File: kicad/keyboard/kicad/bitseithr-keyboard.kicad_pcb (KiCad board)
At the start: 4 copper layers, 365 x 206 mm, 105 parts, among them P2 KEYB CONN 1

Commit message: removed inner layers, added ground plane on bottom
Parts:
- removed U? (x2): SW-TH_EC11E1820402, clholm-kicad-library:SW-TH_EC11E1820402
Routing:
- net GND: track 244.3 -> 217.0 mm, vias 0 -> 2
- net +9V: track 387.4 -> 375.4 mm, vias 3 -> 1
- net COL6: track 226.5 -> 216.3 mm
- net ROW5: track 115.9 -> 106.4 mm
- net ROW3: track 507.2 -> 498.7 mm
- added copper zone on B.Cu, net GND
- removed copper zone on In1.Cu, net (none)
- removed copper zone on In2.Cu, net (none)
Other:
- copper layers 4 -> 2

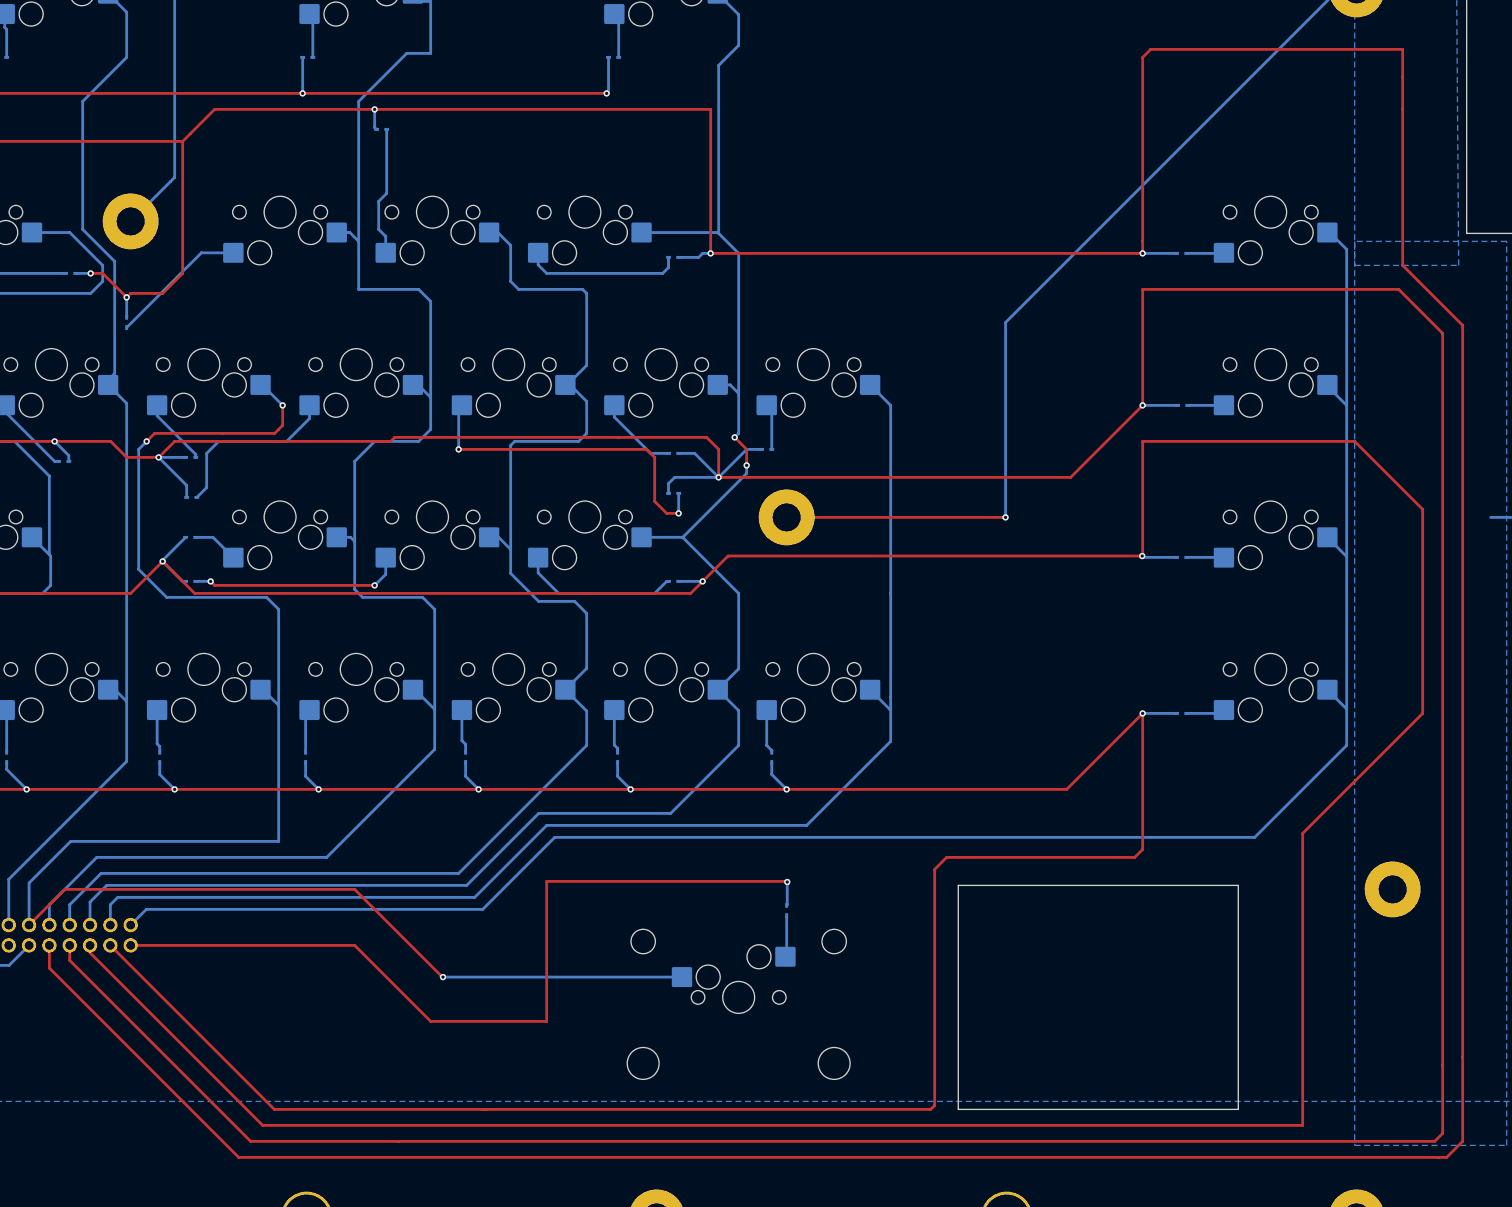
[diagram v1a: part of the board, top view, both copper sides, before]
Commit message: some routing updates
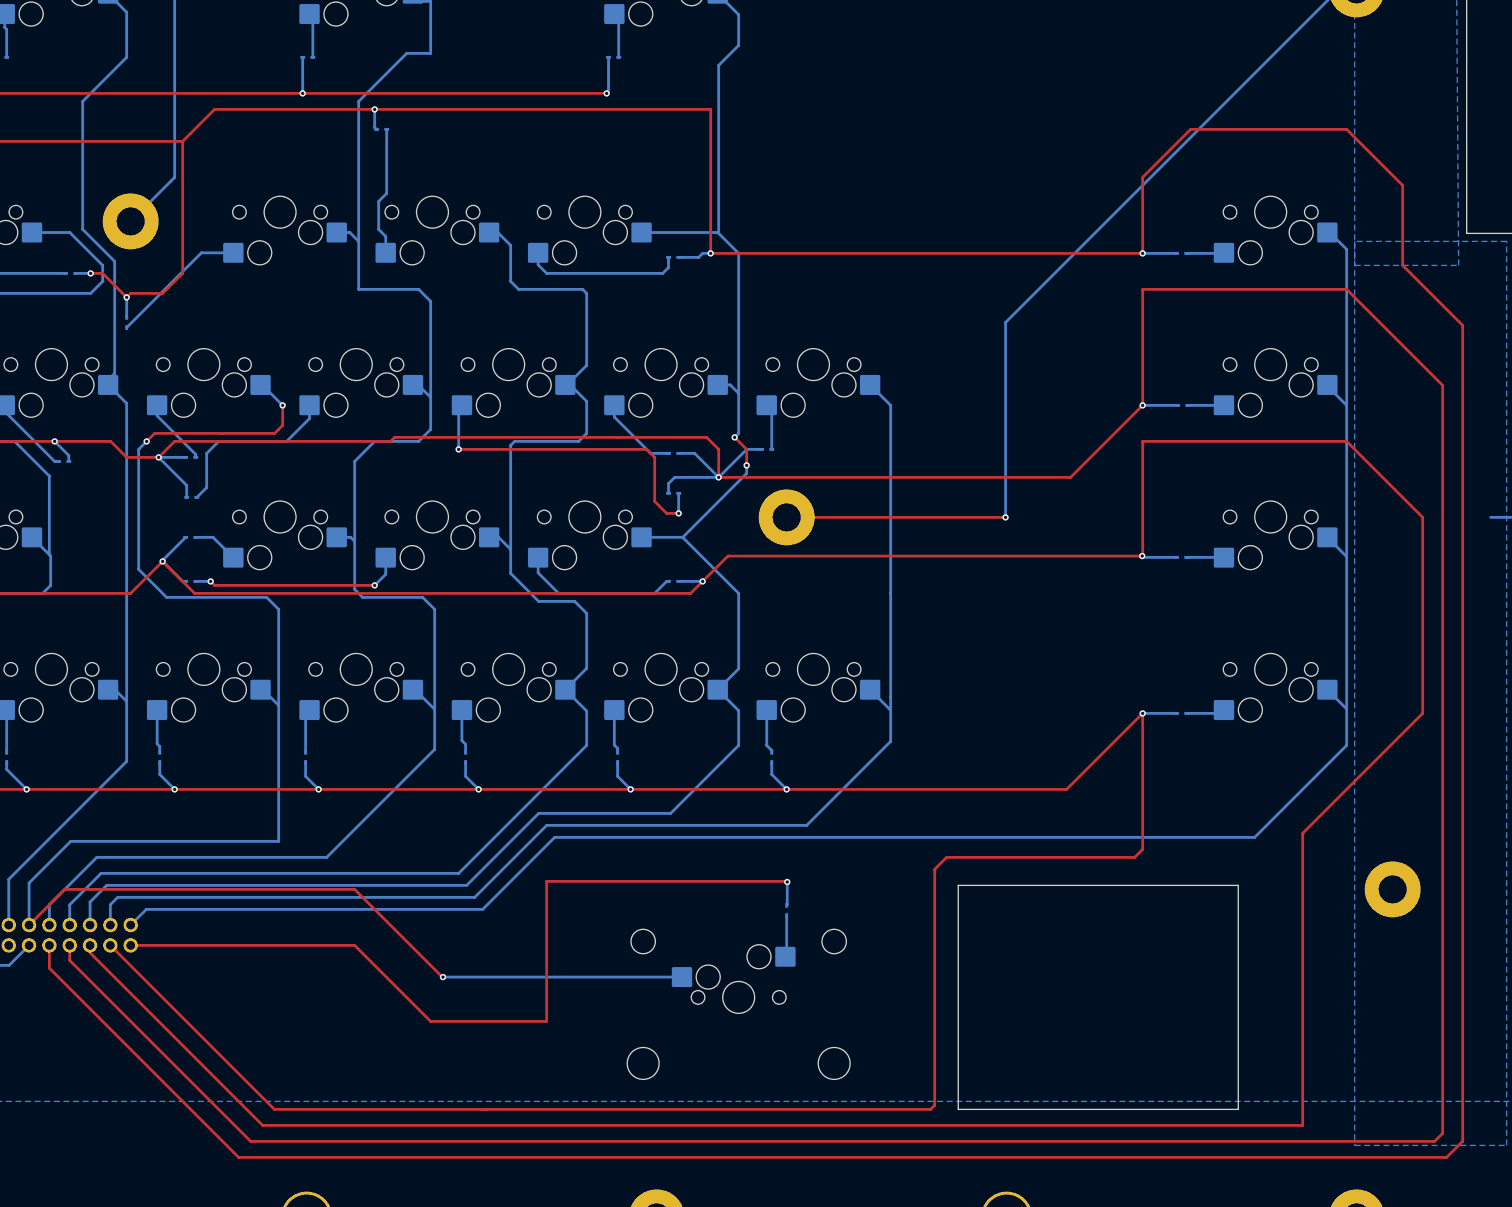
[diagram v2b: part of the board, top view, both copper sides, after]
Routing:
- net ROW1: track 651.7 -> 624.7 mm
- net ROW2: track 573.3 -> 569.5 mm
- net ROW3: track 498.7 -> 498.2 mm
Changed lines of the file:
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@@
 	)
 	(segment
-		(start 99.84 222.34)
-		(end 123.5 246)
+		(start 276.5 142)
+		(end 276.5 244)
 		(width 0.35)
 		(layer "F.Cu")
@@
 	)
 	(segment
-		(start 236.5 131.5)
-		(end 236.5 133)
+		(start 236.5 133)
+		(end 236.5 123.5)
 		(width 0.35)
 		(layer "F.Cu")
@@
 	)
 	(segment
-		(start 273.5 246)
-		(end 274.5 246)
-		(width 0.35)
-		(layer "F.Cu")
-		(net 3)
-	)
-	(segment
-		(start 274.5 246)
-		(end 276.5 244)
+		(start 236.5 123.5)
+		(end 242.5 117.5)
 		(width 0.35)
 		(layer "F.Cu")
@@
 	)
 	(segment
-		(start 269 134.5)
-		(end 269 115)
-		(width 0.35)
-		(layer "F.Cu")
-		(net 3)
-	)
-	(segment
-		(start 276.5 244)
-		(end 276.5 233.5)
-		(width 0.35)
-		(layer "F.Cu")
-		(net 3)
-	)
-	(segment
 		(start 110 138)
 		(end 109.5 138.5)
@@
 	)
 	(segment
-		(start 236.5 108.5)
-		(end 236.5 131.5)
+		(start 269 124.5)
+		(end 269 134.5)
+		(width 0.35)
+		(layer "F.Cu")
+		(net 3)
+	)
+	(segment
+		(start 276.5 244)
+		(end 274.5 246)
 		(width 0.35)
 		(layer "F.Cu")
@@
 	)
 	(segment
+		(start 242.5 117.5)
+		(end 262 117.5)
+		(width 0.35)
+		(layer "F.Cu")
+		(net 3)
+	)
+	(segment
 		(start 54.5 130.5)
 		(end 58 134)
@@
 	)
 	(segment
-		(start 123.5 246)
-		(end 273.5 246)
-		(width 0.35)
-		(layer "F.Cu")
-		(net 3)
-	)
-	(segment
-		(start 276.5 233.5)
-		(end 276.5 142)
-		(width 0.35)
-		(layer "F.Cu")
-		(net 3)
-	)
-	(segment
 		(start 117.5 118)
 		(end 116.5 119)
@@
 	)
 	(segment
-		(start 271 136.5)
-		(end 269 134.5)
-		(width 0.35)
-		(layer "F.Cu")
-		(net 3)
-	)
-	(segment
 		(start 182.5 133)
 		(end 182.5 115)
@@
 	)
 	(segment
-		(start 276.5 142)
-		(end 271 136.5)
-		(width 0.35)
-		(layer "F.Cu")
-		(net 3)
-	)
-	(segment
-		(start 269 115)
-		(end 269 111)
-		(width 0.35)
-		(layer "F.Cu")
-		(net 3)
-	)
-	(segment
-		(start 237.5 107.5)
-		(end 236.5 108.5)
-		(width 0.35)
-		(layer "F.Cu")
-		(net 3)
-	)
-	(segment
 		(start 54.5 122.5)
 		(end 54.5 130.5)
@@
 	)
 	(segment
-		(start 269 111)
-		(end 269 107.5)
-		(width 0.35)
-		(layer "F.Cu")
-		(net 3)
-	)
-	(segment
-		(start 269 107.5)
-		(end 237.5 107.5)
+		(start 99.84 222.34)
+		(end 99.84 219.5)
 		(width 0.35)
 		(layer "F.Cu")
@@
 	)
 	(segment
+		(start 269 134.5)
+		(end 276.5 142)
+		(width 0.35)
+		(layer "F.Cu")
+		(net 3)
+	)
+	(segment
 		(start 113 138)
 		(end 110 138)
@@
 	)
 	(segment
-		(start 99.84 219.5)
+		(start 123.5 246)
 		(end 99.84 222.34)
+		(width 0.35)
+		(layer "F.Cu")
+		(net 3)
+	)
+	(segment
+		(start 274.5 246)
+		(end 123.5 246)
 		(width 0.35)
 		(layer "F.Cu")
@@
 		(net 3)
 	)
+	(segment
+		(start 262 117.5)
+		(end 269 124.5)
+		(width 0.35)
+		(layer "F.Cu")
+		(net 3)
+	)
 	(via
 		(at 105 135.5)
@@
 	)
 	(segment
-		(start 274 243)
-		(end 274 234.5)
-		(width 0.35)
-		(layer "F.Cu")
-		(net 5)
-	)
-	(segment
-		(start 143.5 244)
-		(end 273 244)
-		(width 0.35)
-		(layer "F.Cu")
-		(net 5)
-	)
-	(segment
-		(start 274 143)
-		(end 268.5 137.5)
+		(start 236.5 137.5)
+		(end 262 137.5)
+		(width 0.35)
+		(layer "F.Cu")
+		(net 5)
+	)
+	(segment
+		(start 273 244)
+		(end 125 244)
 		(width 0.35)
 		(layer "F.Cu")
@@
 	)
 	(segment
-		(start 268.5 137.5)
-		(end 236.5 137.5)
+		(start 274 243)
+		(end 273 244)
+		(width 0.35)
+		(layer "F.Cu")
+		(net 5)
+	)
+	(segment
+		(start 274 149.5)
+		(end 274 243)
 		(width 0.35)
 		(layer "F.Cu")
@@
 	)
 	(segment
-		(start 125 244)
-		(end 143.5 244)
-		(width 0.35)
-		(layer "F.Cu")
-		(net 5)
-	)
-	(segment
 		(start 107.5 156.5)
 		(end 100.5 156.5)
@@
 	)
 	(segment
-		(start 102.38 219.5)
+		(start 125 244)
 		(end 102.38 221.38)
-		(width 0.35)
-		(layer "F.Cu")
-		(net 5)
-	)
-	(segment
-		(start 102.38 221.38)
-		(end 125 244)
 		(width 0.35)
 		(layer "F.Cu")
@@
 	)
 	(segment
-		(start 273 244)
-		(end 274 243)
-		(width 0.35)
-		(layer "F.Cu")
-		(net 5)
-	)
-	(segment
 		(start 109.5 158.5)
 		(end 107.5 156.5)
@@
 	)
 	(segment
+		(start 262 137.5)
+		(end 274 149.5)
+		(width 0.35)
+		(layer "F.Cu")
+		(net 5)
+	)
+	(segment
 		(start 236.5 152)
 		(end 227.5 161)
@@
 	)
 	(segment
+		(start 102.38 221.38)
+		(end 102.38 219.5)
+		(width 0.35)
+		(layer "F.Cu")
+		(net 5)
+	)
+	(segment
 		(start 113.5 158.5)
 		(end 109.5 158.5)
@@
 	)
 	(segment
-		(start 236.5 137.5)
-		(end 236.5 152)
+		(start 236.5 152)
+		(end 236.5 137.5)
 		(width 0.35)
 		(layer "F.Cu")
@@
 	)
 	(segment
-		(start 274 234.5)
-		(end 274 143)
-		(width 0.35)
-		(layer "F.Cu")
-		(net 5)
-	)
-	(segment
 		(start 142.5 156.5)
 		(end 115.5 156.5)
@@
 	(segment
 		(start 271.5 190.5)
-		(end 271.5 165)
-		(width 0.35)
-		(layer "F.Cu")
-		(net 7)
-	)
-	(segment
-		(start 263 156.5)
+		(end 271.5 166)
+		(width 0.35)
+		(layer "F.Cu")
+		(net 7)
+	)
+	(segment
+		(start 262 156.5)
 		(end 236.5 156.5)
 		(width 0.35)
@@
 	)
 	(segment
-		(start 271.5 165)
-		(end 263 156.5)
-		(width 0.35)
-		(layer "F.Cu")
+		(start 262 156.5)
+		(end 271.5 166)
+		(width 0.35)
+		(layer "F.Cu")

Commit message: drc fixes
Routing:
- net ROW4: track 405.5 -> 405.0 mm
- net GND: track 217.0 -> 216.5 mm
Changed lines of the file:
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@@
-	(segment
-		(start 154 240)
-		(end 154.5 240)
-		(width 0.35)
-		(layer "F.Cu")
-		(net 9)
-	)
 	(segment
 		(start 154 240)
@@
 		(width 0.35)
 		(layer "F.Cu")
-		(net 42)
-	)
-	(segment
-		(start 54.5 222)
-		(end 54 222)
-		(width 0.35)
-		(layer "F.Cu")

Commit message: wavy traces :wave:
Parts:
- moved R15 3.34 mm to (211.5, 88.5)
- moved D10 1.50 mm to (77.4, 196.1)
- moved D11 1.50 mm to (95.4, 108.5)
- moved D12 1.50 mm to (103.1, 159.0)
- moved D13 1.50 mm to (96.0, 196.0)
- moved D14 1.50 mm to (119.0, 158.5)
- moved D15 1.50 mm to (115.1, 196.0)
- moved D16 1.50 mm to (193.5, 215.1)
- moved D17 1.50 mm to (133.6, 108.5)
- moved D18 1.50 mm to (111.0, 141.6)
- moved D19 1.50 mm to (119.1, 163.5)
- moved D2 1.50 mm to (57.4, 108.5)
- moved D20 1.50 mm to (119.0, 168.5)
- moved D21 1.50 mm to (133.4, 196.0)
- moved D22 1.50 mm to (142.9, 117.5)
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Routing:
- net COL8: track 237.0 -> 252.7 mm
- net COL4: track 196.4 -> 201.7 mm
- net ROW3: track 498.2 -> 493.9 mm
- net ROW2: track 569.5 -> 565.6 mm
- net ROW1: track 624.7 -> 621.5 mm
- net Net-(R15-Pad1): track 14.1 -> 11.1 mm
- net COL6: track 216.3 -> 213.7 mm
- net ROW5: track 106.4 -> 104.0 mm
- net COL5: track 173.3 -> 170.9 mm
- net +9V: track 375.4 -> 373.4 mm
- net ROW0: track 278.0 -> 276.1 mm
- net COL1: track 132.3 -> 134.2 mm
- net Net-(D37-A): track 96.5 -> 98.3 mm
- net ROW4: track 405.0 -> 403.4 mm
- net COL7: track 157.7 -> 156.5 mm
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
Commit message: fixed drc warning
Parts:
- HOLE (x17): footprint MountingHole:MountingHole_3.5mm -> clholm-kicad-library:MountingHole_M3_GND_7mm
- HOLE (x12): footprint MountingHole:MountingHole_5.7mm -> clholm-kicad-library:MountingHole_5.7mm
